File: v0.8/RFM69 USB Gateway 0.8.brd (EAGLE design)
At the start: 40.7 x 17.3 mm, 25 parts, among them CN1 MINIB, IC3 MCP1703, U2 ATMEGA328P-MU, X1 16 MHz

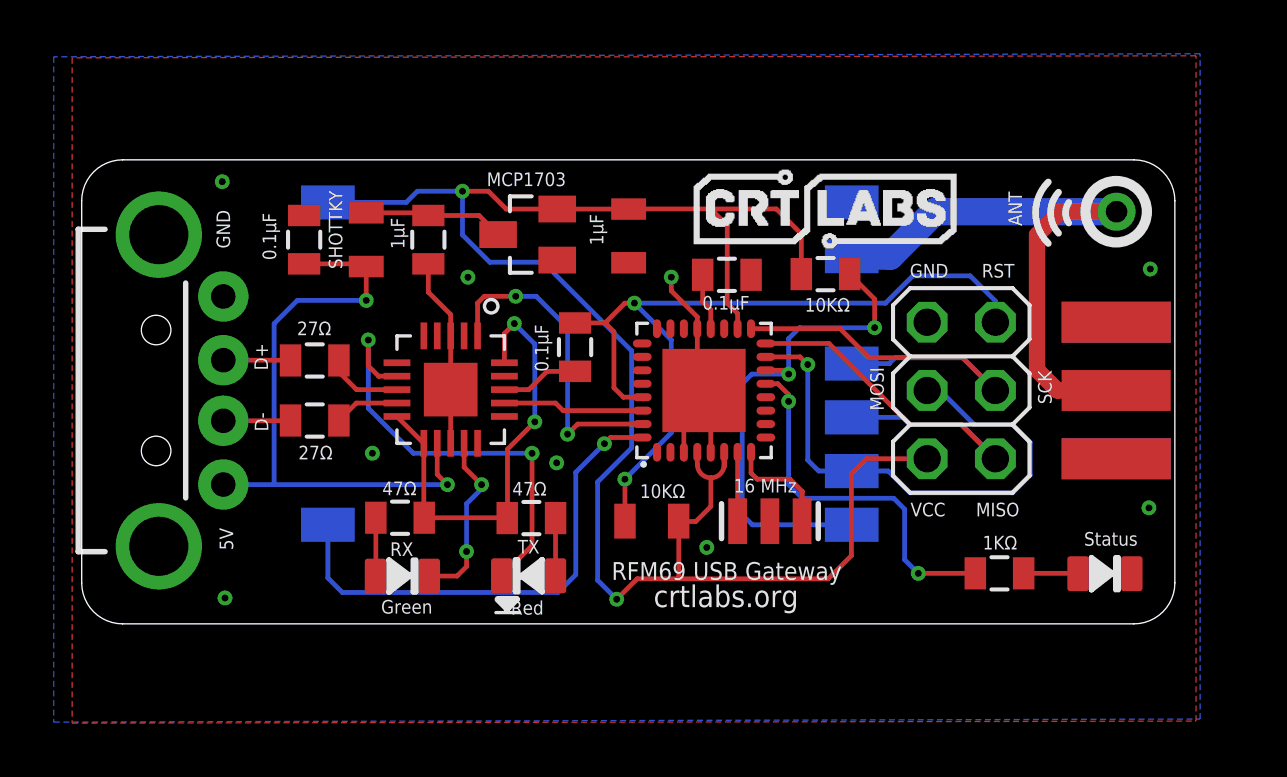
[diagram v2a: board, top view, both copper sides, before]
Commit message: Adjusted silkscreen
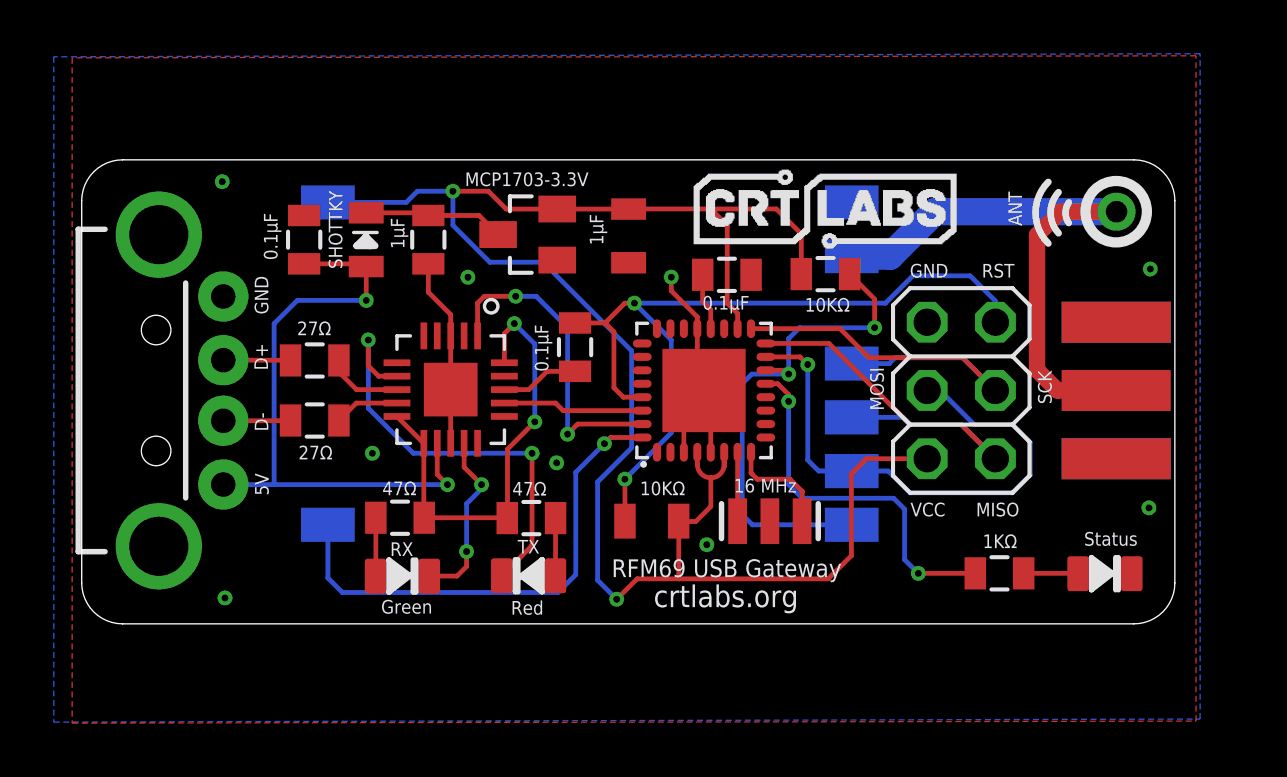
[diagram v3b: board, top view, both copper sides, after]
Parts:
- IC3: value MCP1703 -> MCP1703-3.3V
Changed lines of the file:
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@@
 <text x="51.6382" y="4.0894" size="1.016" layer="22" font="vector" ratio="15" rot="MR0">Akram Ali</text>
 <text x="13.462" y="11.5697" size="0.8128" layer="22" font="vector" ratio="9" rot="MR270" align="bottom-center">v0.8    2016</text>
-<text x="17.6149" y="16.8656" size="0.508" layer="121" font="vector" rot="R90">GND</text>
+<text x="18.5293" y="15.8496" size="0.508" layer="121" font="vector" rot="R270">GND</text>
 <text x="19.0246" y="12.3317" size="0.508" layer="121" font="vector" rot="R90">D+</text>
 <text x="19.0373" y="10.0584" size="0.508" layer="121" font="vector" rot="R90">D-</text>
-<text x="17.7292" y="5.6388" size="0.508" layer="121" font="vector" rot="R90">5V</text>
-<wire x1="27.5844" y1="3.81" x2="27.9273" y2="3.4671" width="0.254" layer="21"/>
-<wire x1="27.9273" y1="3.4671" x2="28.2702" y2="3.81" width="0.254" layer="21"/>
-<wire x1="28.2702" y1="3.81" x2="27.7749" y2="3.81" width="0.254" layer="21"/>
-<wire x1="27.6606" y1="3.81" x2="27.7749" y2="3.81" width="0.254" layer="21"/>
-<wire x1="27.7749" y1="3.81" x2="27.9654" y2="3.6195" width="0.254" layer="21"/>
-<wire x1="28.3845" y1="3.3147" x2="27.5082" y2="3.3147" width="0.127" layer="21"/>
+<text x="19.05" y="7.6708" size="0.508" layer="121" font="vector" rot="SR90">5V</text>
+<wire x1="23.0124" y1="16.9672" x2="22.6695" y2="17.3101" width="0.254" layer="21"/>
+<wire x1="22.6695" y1="17.3101" x2="22.3266" y2="16.9672" width="0.254" layer="21"/>
+<wire x1="22.3266" y1="16.9672" x2="22.8219" y2="16.9672" width="0.254" layer="21"/>
+<wire x1="22.9362" y1="16.9672" x2="22.8219" y2="16.9672" width="0.254" layer="21"/>
+<wire x1="22.8219" y1="16.9672" x2="22.6314" y2="17.1577" width="0.254" layer="21"/>
+<wire x1="22.2123" y1="17.4625" x2="23.0886" y2="17.4625" width="0.127" layer="21"/>
 <text x="45.593" y="15.7861" size="0.508" layer="121" font="vector" ratio="10">RST</text>
 <text x="42.9133" y="15.7861" size="0.508" layer="121" font="vector" ratio="10">GND</text>
@@
 <text x="41.9481" y="10.8331" size="0.508" layer="121" font="vector" ratio="10" rot="R90">MOSI</text>
 <text x="47.6885" y="12.319" size="0.508" layer="121" font="vector" ratio="10" rot="R270">SCK</text>
-<text x="31.8135" y="4.5339" size="0.6604" layer="21" font="vector" ratio="7">RFM69 USB Gateway</text>
+<text x="31.8135" y="4.6355" size="0.6604" layer="21" font="vector" ratio="7">RFM69 USB Gateway</text>
 <text x="33.3756" y="3.5179" size="0.8128" layer="21" font="vector" ratio="12">crtlabs.org</text>
 <text x="46.5836" y="18.9865" size="0.508" layer="21" font="vector" rot="R270">ANT</text>
@@
 <attribute name="VALUE" x="36.3601" y="7.7851" size="0.508" layer="121" font="vector"/>
 </element>
-<element name="IC3" library="linear" package="SOT23" value="MCP1703" x="28.6893" y="17.3863" smashed="yes" rot="R90">
-<attribute name="VALUE" x="27.1653" y="19.1897" size="0.508" layer="121" font="vector"/>
+<element name="IC3" library="linear" package="SOT23" value="MCP1703-3.3V" x="28.6893" y="17.3863" smashed="yes" rot="R90">
+<attribute name="VALUE" x="26.3525" y="19.1897" size="0.508" layer="121" font="vector"/>
 </element>
 <element name="C5" library="SparkFun" package="0805" value="0.1μF" x="36.1061" y="15.8877" smashed="yes">
@@
 </element>
 <element name="R1" library="LowPowerLab" package="0805" value="10KΩ" x="33.3121" y="6.7183" smashed="yes">
-<attribute name="VALUE" x="34.5567" y="8.0899" size="0.508" layer="121" font="vector" rot="R180"/>
+<attribute name="VALUE" x="34.5567" y="8.1915" size="0.508" layer="121" font="vector" rot="R180"/>
 </element>
 <element name="C4" library="LowPowerLab" package="0805" value="1μF" x="32.4485" y="17.3355" smashed="yes" rot="R270">
@@
 </element>
 <element name="R2" library="SparkFun" package="0805" value="1KΩ" x="46.2534" y="4.7752" smashed="yes" rot="R180">
-<attribute name="VALUE" x="46.9138" y="6.1722" size="0.508" layer="121" font="vector" rot="R180"/>
+<attribute name="VALUE" x="46.9138" y="6.223" size="0.508" layer="121" font="vector" rot="R180"/>
 </element>
 <element name="U$1" library="LowPowerLab" package="RFM12B-ANTENNA" value="RFM12B_ANTENNA" x="50.6095" y="18.2372"/>
@@
 </element>
 <element name="C6" library="SparkFun" package="0805" value="0.1μF" x="20.3708" y="17.1958" smashed="yes" rot="R90">
-<attribute name="VALUE" x="19.3294" y="16.4338" size="0.508" layer="121" font="vector" rot="R90"/>
+<attribute name="VALUE" x="19.3802" y="16.4338" size="0.508" layer="121" font="vector" rot="R90"/>
 </element>
 <element name="D" library="LowPowerLab" package="0805" value="SHOTTKY" x="22.6822" y="17.1958" smashed="yes" rot="R270">
@@
 <wire x1="25.8252" y1="14.4084" x2="24.9936" y2="15.24" width="0.1778" layer="1"/>
 <wire x1="24.9936" y1="15.24" x2="24.9936" y2="16.2958" width="0.1778" layer="1"/>
-<via x="35.3568" y="5.7404" extent="1-16" drill="0.254" diameter="0.127"/>
+<via x="35.3568" y="5.842" extent="1-16" drill="0.254" diameter="0.127"/>
 <via x="34.036" y="15.7988" extent="1-16" drill="0.254" diameter="0.127"/>
 <wire x1="35.0052" y1="13.8824" x2="35.0052" y2="14.3216" width="0.1778" layer="1"/>
@@
 <wire x1="34.3248" y1="6.7056" x2="34.3121" y2="6.7183" width="0.1778" layer="1"/>
 <wire x1="29.7893" y1="18.3363" x2="27.8917" y2="18.3363" width="0.1778" layer="1"/>
-<via x="26.2636" y="18.9992" extent="1-16" drill="0.254" diameter="0.127"/>
+<via x="25.908" y="18.9992" extent="1-16" drill="0.254" diameter="0.127"/>
 <wire x1="21.2533" y1="18.5824" x2="24.1704" y2="18.5824" width="0.1778" layer="16"/>
 <wire x1="43.561" y1="9.0424" x2="41.3004" y2="9.0424" width="0.1778" layer="1"/>
@@
 <wire x1="34.3408" y1="4.572" x2="39.878" y2="4.572" width="0.1778" layer="1"/>
 <wire x1="34.3154" y1="4.5974" x2="34.3408" y2="4.572" width="0.1778" layer="1"/>
-<wire x1="24.5872" y1="18.9992" x2="26.2636" y2="18.9992" width="0.1778" layer="16"/>
 <wire x1="27.8917" y1="18.3363" x2="27.2288" y2="18.9992" width="0.1778" layer="1"/>
-<wire x1="27.2288" y1="18.9992" x2="26.2636" y2="18.9992" width="0.1778" layer="1"/>
-<wire x1="26.2636" y1="18.9992" x2="26.2636" y2="17.3736" width="0.1778" layer="16"/>
-<wire x1="26.2636" y1="17.3736" x2="27.2796" y2="16.3576" width="0.1778" layer="16"/>
+<wire x1="25.908" y1="17.7292" x2="27.2796" y2="16.3576" width="0.1778" layer="16"/>
 <wire x1="32.5628" y1="9.4488" x2="32.5628" y2="13.0556" width="0.1778" layer="16"/>
 <wire x1="32.766" y1="4.572" x2="32.004" y2="3.81" width="0.1778" layer="1"/>
@@
 <wire x1="31.2928" y1="8.1788" x2="31.2928" y2="4.5212" width="0.1778" layer="16"/>
 <wire x1="31.2928" y1="4.5212" x2="32.004" y2="3.81" width="0.1778" layer="16"/>
+<wire x1="27.2288" y1="18.9992" x2="25.908" y2="18.9992" width="0.1778" layer="1"/>
+<wire x1="24.5872" y1="18.9992" x2="25.908" y2="18.9992" width="0.1778" layer="16"/>
+<wire x1="25.908" y1="18.9992" x2="25.908" y2="17.7292" width="0.1778" layer="16"/>
 </signal>
 <signal name="D9">
